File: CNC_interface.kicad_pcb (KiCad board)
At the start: 2 copper layers, 86.4 x 99.1 mm, 35 parts, among them J1 Conn_01x04_Male, J10 Conn_01x08, J11 Conn_01x08, J12 Conn_01x08, J13 Conn_01x08, J14 Conn_01x03_Male, J15 Conn_01x03_Male, J16 Conn_01x03_Male, J17 Conn_01x08, J18 Conn_01x10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

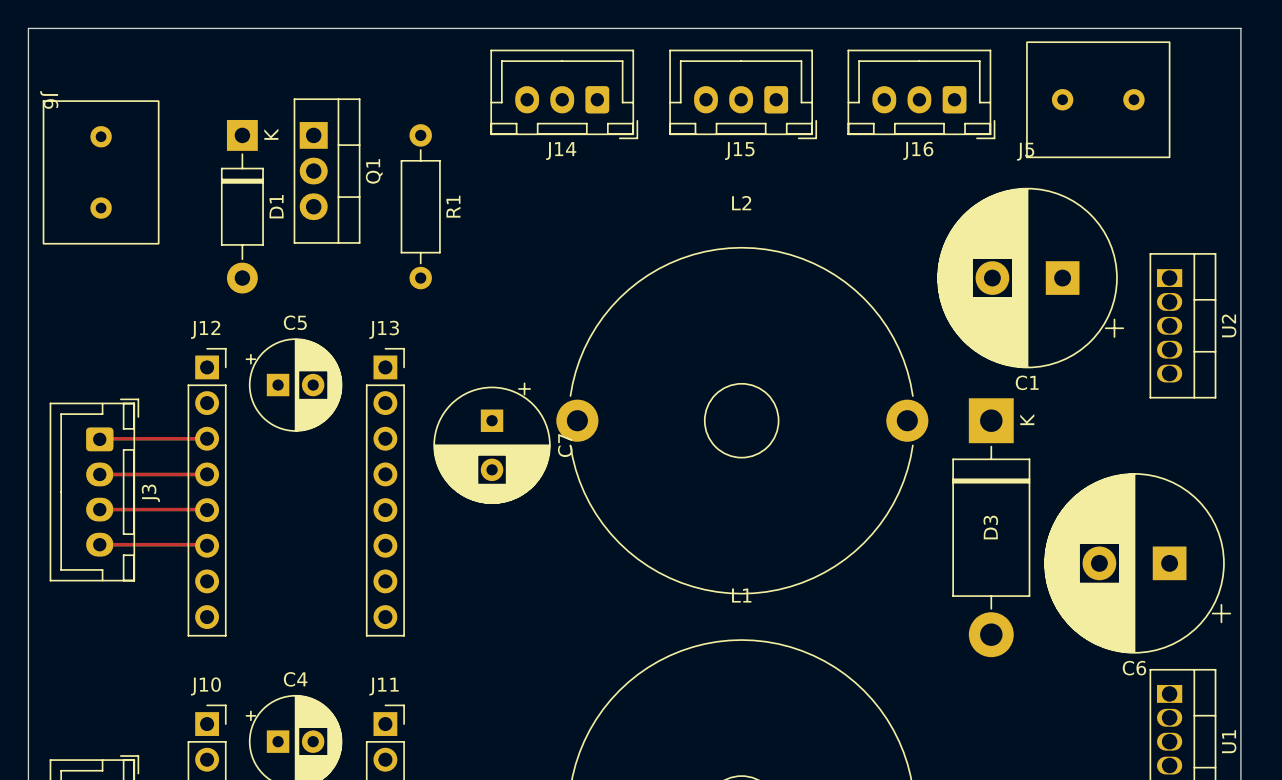
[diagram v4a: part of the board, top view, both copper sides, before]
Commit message: place first traces
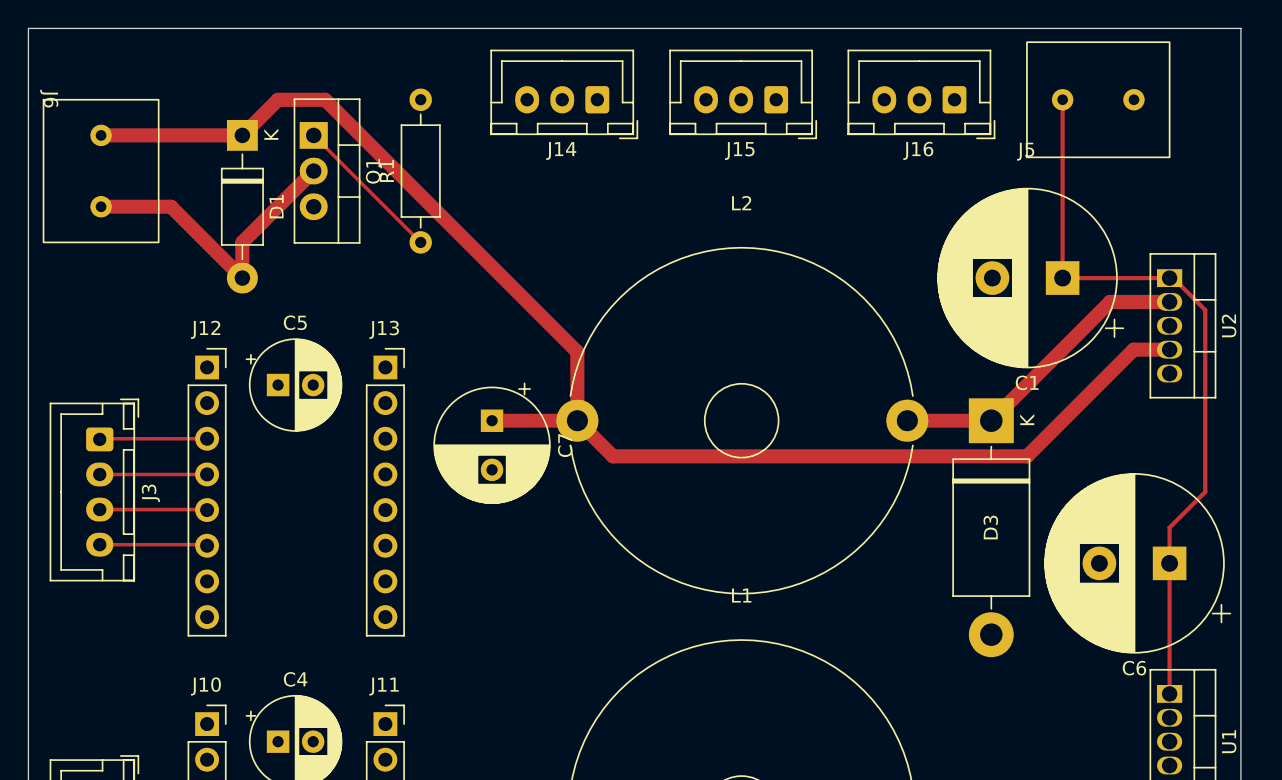
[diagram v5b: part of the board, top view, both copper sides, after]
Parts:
- moved R1 7.62 mm to (73.7, 45.7), turned to 90 degrees
- moved J6 0.09 mm to (46.8, 35.6)
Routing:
- net +12V: track 0.00 -> 99.8 mm
- net +24V: track 0.00 -> 52.2 mm
- net Net-(D3-Pad1): track 0.00 -> 22.2 mm
- net DC-: track 0.00 -> 21.9 mm
- net DCtrl: track 0.00 -> 10.8 mm
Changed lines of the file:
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@@
   )
   (setup
+    (stackup
+      (layer "F.SilkS" (type "Top Silk Screen"))
+      (layer "F.Paste" (type "Top Solder Paste"))
+      (layer "F.Mask" (type "Top Solder Mask") (thickness 0.01))
+      (layer "F.Cu" (type "copper") (thickness 0.035))
+      (layer "dielectric 1" (type "core") (thickness 1.51) (material "FR4") (epsilon_r 4.5) (loss_tangent 0.02))
+      (layer "B.Cu" (type "copper") (thickness 0.035))
+      (layer "B.Mask" (type "Bottom Solder Mask") (thickness 0.01))
+      (layer "B.Paste" (type "Bottom Solder Paste"))
+      (layer "B.SilkS" (type "Bottom Silk Screen"))
+      (copper_finish "None")
+      (dielectric_constraints no)
+    )
     (pad_to_mask_clearance 0)
     (pcbplotparams
@@
   )
   (footprint "CNC_interface:RS_pro_screw_terminal_P5.08_x2" (layer "F.Cu")
-    (at 46.795 35.655 -90)
+    (at 46.795 35.56 -90)
     (property "Sheetfile" "CNC_interface.kicad_sch")
     (property "Sheetname" "")
@@
   )
   (footprint "Resistor_THT:R_Axial_DIN0207_L6.3mm_D2.5mm_P10.16mm_Horizontal" (layer "F.Cu")
-    (at 73.66 38.1 -90)
+    (at 73.66 45.72 90)
     (descr "Resistor, Axial_DIN0207 series, Axial, Horizontal, pin pitch=10.16mm, 0.25W = 1/4W, length*diameter=6.3*2.5mm^2, http://cdn-reichelt.de/documents/datenblatt/B400/1_4W%23YAG.pdf")
     (tags "Resistor Axial_DIN0207 series Axial Horizontal pin pitch 10.16mm 0.25W = 1/4W length 6.3mm diameter 2.5mm")
@@
     (fp_line (start 0 0) (end 1.93 0) (layer "F.Fab") (width 0.1))
     (fp_line (start 1.93 -1.25) (end 1.93 1.25) (layer "F.Fab") (width 0.1))
-    (pad "1" thru_hole circle (at 0 0 270) (size 1.6 1.6) (drill 0.8) (layers *.Cu *.Mask)
+    (pad "1" thru_hole circle (at 0 0 90) (size 1.6 1.6) (drill 0.8) (layers *.Cu *.Mask)
       (net 41 "DCtrl") (pintype "passive"))
-    (pad "2" thru_hole oval (at 10.16 0 270) (size 1.6 1.6) (drill 0.8) (layers *.Cu *.Mask)
+    (pad "2" thru_hole oval (at 10.16 0 90) (size 1.6 1.6) (drill 0.8) (layers *.Cu *.Mask)
       (net 19 "GND") (pintype "passive"))
     (model "${KICAD6_3DMODEL_DIR}/Resistor_THT.3dshapes/R_Axial_DIN0207_L6.3mm_D2.5mm_P10.16mm_Horizontal.wrl"
@@
   (gr_line (start 45.72 129.54) (end 45.72 30.48) (layer "Edge.Cuts") (width 0.05))
   (gr_line (start 132.08 30.48) (end 132.08 129.54) (layer "Edge.Cuts") (width 0.05))
+  (segment (start 50.895 43.18) (end 55.88 43.18) (width 1) (layer "F.Cu") (net 1))
+  (segment (start 66.04 40.64) (end 60.96 45.72) (width 1) (layer "F.Cu") (net 1))
+  (segment (start 55.88 43.18) (end 60.96 48.26) (width 1) (layer "F.Cu") (net 1))
+  (segment (start 60.96 45.72) (end 60.96 48.26) (width 1) (layer "F.Cu") (net 1))
   (segment (start 50.8 119.26) (end 58.325 119.26) (width 0.25) (layer "F.Cu") (net 3))
   (segment (start 58.325 119.26) (end 58.445 119.38) (width 0.25) (layer "F.Cu") (net 3))
@@
   (segment (start 50.8 114.26) (end 58.405 114.26) (width 0.25) (layer "F.Cu") (net 5))
   (segment (start 50.8 111.76) (end 58.445 111.76) (width 0.25) (layer "F.Cu") (net 6))
+  (segment (start 127 48.26) (end 127.2625 48.26) (width 0.3) (layer "F.Cu") (net 8))
+  (segment (start 127.2625 48.26) (end 129.54 50.5375) (width 0.3) (layer "F.Cu") (net 8))
+  (segment (start 129.54 50.5375) (end 129.54 63.5) (width 0.3) (layer "F.Cu") (net 8))
+  (segment (start 119.38 35.56) (end 119.38 48.26) (width 0.3) (layer "F.Cu") (net 8))
+  (segment (start 129.54 63.5) (end 127 66.04) (width 0.3) (layer "F.Cu") (net 8))
+  (segment (start 127 66.04) (end 127 68.58) (width 0.3) (layer "F.Cu") (net 8))
+  (segment (start 127 77.88) (end 127 68.58) (width 0.3) (layer "F.Cu") (net 8))
+  (segment (start 119.38 48.26) (end 127 48.26) (width 0.3) (layer "F.Cu") (net 8))
+  (segment (start 114.3 58.42) (end 108.32 58.42) (width 1) (layer "F.Cu") (net 9))
+  (segment (start 122.76 49.96) (end 114.3 58.42) (width 1) (layer "F.Cu") (net 9))
+  (segment (start 127 49.96) (end 122.76 49.96) (width 1) (layer "F.Cu") (net 9))
   (segment (start 58.37 92.65) (end 58.445 92.725) (width 0.25) (layer "F.Cu") (net 14))
   (segment (start 50.8 92.65) (end 58.37 92.65) (width 0.25) (layer "F.Cu") (net 14))
@@
   (segment (start 50.8 59.75) (end 50.845 59.705) (width 0.25) (layer "F.Cu") (net 27))
   (segment (start 50.845 59.705) (end 58.445 59.705) (width 0.25) (layer "F.Cu") (net 27))
+  (segment (start 73.66 45.72) (end 66.04 38.1) (width 0.25) (layer "F.Cu") (net 41))
+  (segment (start 124.44 53.36) (end 116.84 60.96) (width 1) (layer "F.Cu") (net 61))
+  (segment (start 127 53.36) (end 124.44 53.36) (width 1) (layer "F.Cu") (net 61))
+  (segment (start 84.82 53.528478) (end 66.851522 35.56) (width 1) (layer "F.Cu") (net 61))
+  (segment (start 84.82 58.42) (end 78.74 58.42) (width 1) (layer "F.Cu") (net 61))
+  (segment (start 66.851522 35.56) (end 63.5 35.56) (width 1) (layer "F.Cu") (net 61))
+  (segment (start 87.36 60.96) (end 84.82 58.42) (width 1) (layer "F.Cu") (net 61))
+  (segment (start 60.96 38.1) (end 50.895 38.1) (width 1) (layer "F.Cu") (net 61))
+  (segment (start 116.84 60.96) (end 87.36 60.96) (width 1) (layer "F.Cu") (net 61))
+  (segment (start 63.5 35.56) (end 60.96 38.1) (width 1) (layer "F.Cu") (net 61))
+  (segment (start 84.82 58.42) (end 84.82 53.528478) (width 1) (layer "F.Cu") (net 61))
   (group "" (id 11578d5e-03e8-4330-bf12-98756cee3ec6)
     (members

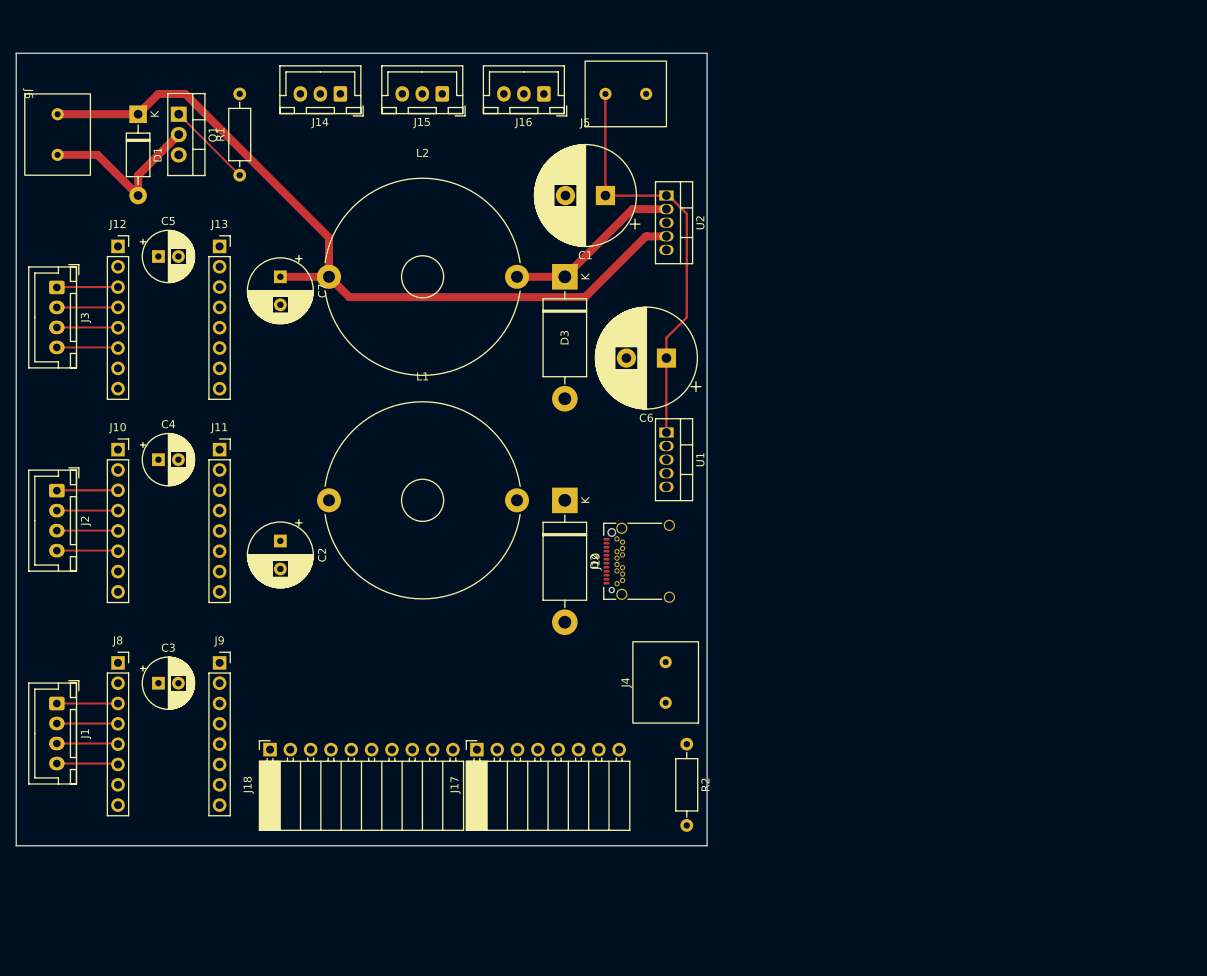
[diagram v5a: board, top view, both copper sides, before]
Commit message: route pcb + GND floorplan
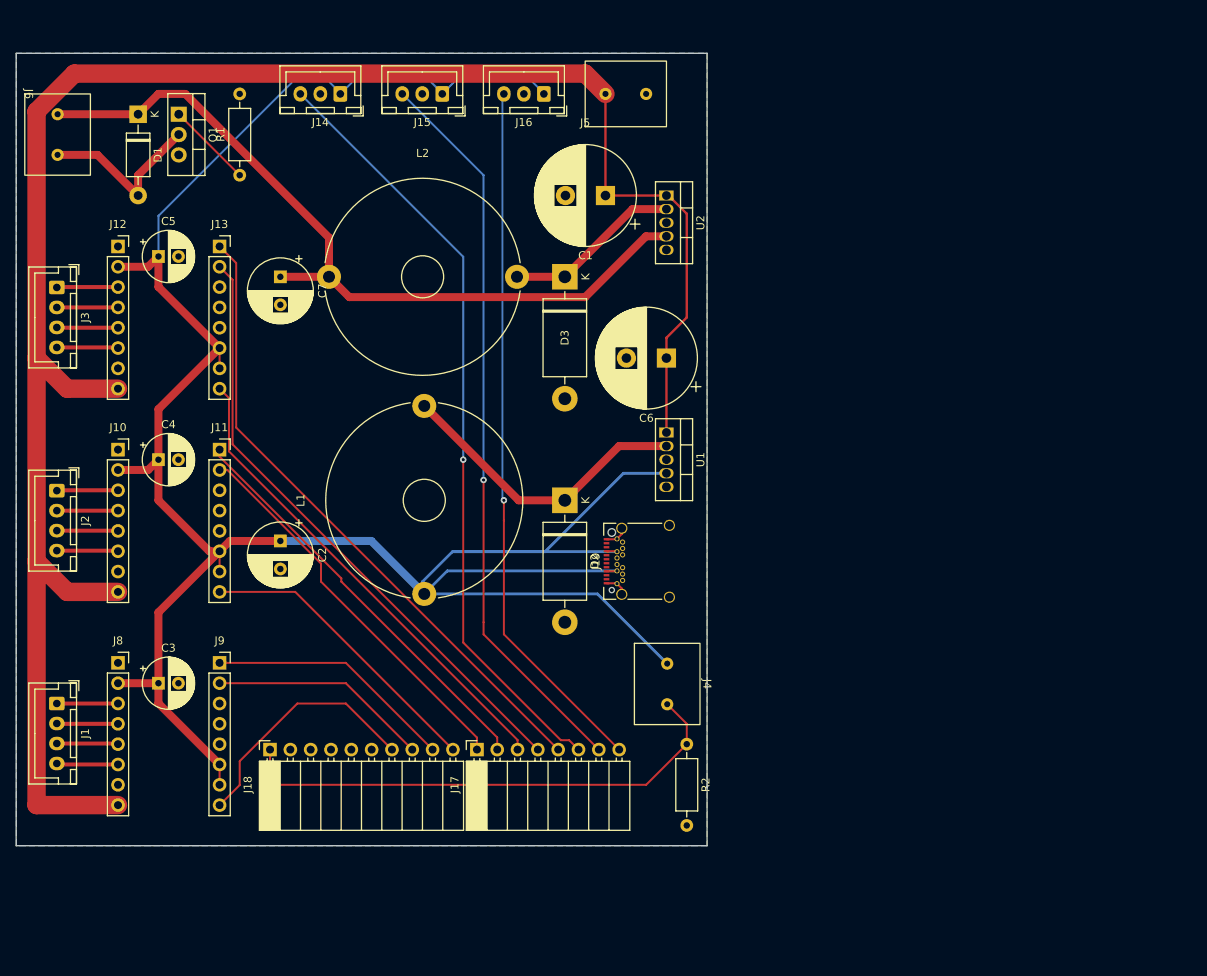
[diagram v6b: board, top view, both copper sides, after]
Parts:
- moved L1 16.7 mm to (96.5, 98.1), turned to 90 degrees
- moved J4 12.8 mm to (123.0, 104.2), turned to -90 degrees
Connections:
- J17 pad 3: ENx -> ENz
- J17 pad 4: STEPx -> STEPz
- J17 pad 5: DIRx -> DIRz
- J18 pad 7: ENz -> ENx
- J18 pad 8: STEPz -> STEPx
- J18 pad 9: DIRz -> DIRx
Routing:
- net +5V: track 0.00 -> 319.0 mm
- net +24V: track 52.2 -> 246.8 mm
- net Lx: track 0.00 -> 97.0 mm, vias 0 -> 1
- net Ly: track 0.00 -> 92.1 mm, vias 0 -> 1
- net Lz: track 0.00 -> 88.1 mm, vias 0 -> 1
- net DIRz: track 0.00 -> 80.4 mm
- net STEPz: track 0.00 -> 76.8 mm
- net CONT: track 0.00 -> 63.8 mm
- net ENz: track 0.00 -> 60.5 mm
- net DIRy: track 0.00 -> 51.9 mm
- net STEPy: track 0.00 -> 48.8 mm
- net Net-(D2-Pad1): track 0.00 -> 38.0 mm
- net ENy: track 0.00 -> 37.3 mm
- net DIRx: track 0.00 -> 31.1 mm
- net ENx: track 0.00 -> 30.9 mm
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- added copper zone on B.Cu, net GND

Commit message: Finish routing
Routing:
- net DCtrl: track 10.8 -> 89.4 mm
- net GND: track 5.82 -> 24.3 mm
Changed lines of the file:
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@@
   (segment (start 69.865 92.725) (end 63.5 86.36) (width 1) (layer "F.Cu") (net 2))
   (segment (start 96.73 98.06) (end 99.61 95.18) (width 0.35) (layer "B.Cu") (net 2))
-  (segment (start 98.98 35.48) (end 98.98 35.56) (width 0.25) (layer "B.Cu") (net 2))
   (segment (start 63.5 55.88) (end 63.5 50.8) (width 0.25) (layer "B.Cu") (net 2))
   (segment (start 96.73 98.06) (end 96.52 97.85) (width 0.35) (layer "B.Cu") (net 2))
-  (segment (start 96.52 33.02) (end 98.98 35.48) (width 0.25) (layer "B.Cu") (net 2))
   (segment (start 118.38 98.06) (end 127.095 106.775) (width 0.35) (layer "B.Cu") (net 2))
   (segment (start 99.61 95.18) (end 120.82 95.18) (width 0.35) (layer "B.Cu") (net 2))
@@
   (segment (start 83.82 33.02) (end 86.24 35.44) (width 0.25) (layer "B.Cu") (net 2))
   (segment (start 86.24 35.44) (end 86.24 35.56) (width 0.25) (layer "B.Cu") (net 2))
+  (segment (start 96.52 33.02) (end 98.98 35.48) (width 0.25) (layer "B.Cu") (net 2))
   (segment (start 81.28 33.02) (end 83.82 33.02) (width 0.25) (layer "B.Cu") (net 2))
+  (segment (start 88.78 33.02) (end 96.52 33.02) (width 0.25) (layer "B.Cu") (net 2))
   (segment (start 96.52 96.52) (end 100.26 92.78) (width 0.35) (layer "B.Cu") (net 2))
-  (segment (start 86.24 35.56) (end 88.78 33.02) (width 0.25) (layer "B.Cu") (net 2))
   (segment (start 96.73 98.06) (end 90.11 91.44) (width 1) (layer "B.Cu") (net 2))
   (segment (start 96.52 97.85) (end 96.52 96.52) (width 0.35) (layer "B.Cu") (net 2))
-  (segment (start 88.78 33.02) (end 96.52 33.02) (width 0.25) (layer "B.Cu") (net 2))
+  (segment (start 86.24 35.56) (end 88.78 33.02) (width 0.25) (layer "B.Cu") (net 2))
   (segment (start 109.22 33.02) (end 111.68 35.48) (width 0.25) (layer "B.Cu") (net 2))
   (segment (start 111.68 35.48) (end 111.68 35.56) (width 0.25) (layer "B.Cu") (net 2))
   (segment (start 111.829022 92.78) (end 121.629022 82.98) (width 0.35) (layer "B.Cu") (net 2))
+  (segment (start 98.98 35.48) (end 98.98 35.56) (width 0.25) (layer "B.Cu") (net 2))
   (segment (start 58.445 119.38) (end 50.8 119.38) (width 0.5) (layer "F.Cu") (net 3))
   (segment (start 58.325 119.26) (end 58.445 119.38) (width 0.25) (layer "F.Cu") (net 3))
@@
   (segment (start 100.31 117.52) (end 80.595 97.805) (width 0.25) (layer "F.Cu") (net 18))
   (segment (start 80.595 97.805) (end 71.145 97.805) (width 0.25) (layer "F.Cu") (net 18))
+  (segment (start 96.48 35.56) (end 99.02 38.1) (width 0.25) (layer "F.Cu") (net 19))
   (segment (start 120.77 96.73) (end 120.82 96.78) (width 0.25) (layer "F.Cu") (net 19))
   (segment (start 119.51 96.73) (end 120.77 96.73) (width 0.25) (layer "F.Cu") (net 19))
+  (segment (start 99.02 38.1) (end 106.64 38.1) (width 0.25) (layer "F.Cu") (net 19))
   (segment (start 121.42 97.38) (end 121.42 98.11) (width 0.25) (layer "F.Cu") (net 19))
   (segment (start 119.51 91.23) (end 120.77 91.23) (width 0.25) (layer "F.Cu") (net 19))
   (segment (start 120.82 96.78) (end 121.42 97.38) (width 0.25) (layer "F.Cu") (net 19))
   (segment (start 121.42 90.58) (end 121.42 89.85) (width 0.25) (layer "F.Cu") (net 19))
+  (segment (start 106.64 38.1) (end 109.18 35.56) (width 0.25) (layer "F.Cu") (net 19))
   (segment (start 120.82 91.18) (end 121.42 90.58) (width 0.25) (layer "F.Cu") (net 19))
   (segment (start 120.77 91.23) (end 120.82 91.18) (width 0.25) (layer "F.Cu") (net 19))
+  (segment (start 83.74 35.56) (end 83.82 35.56) (width 0.25) (layer "B.Cu") (net 19))
+  (segment (start 83.82 35.56) (end 86.36 38.1) (width 0.25) (layer "B.Cu") (net 19))
   (segment (start 103.31 117.52) (end 103.31 116.01) (width 0.25) (layer "F.Cu") (net 22))
   (segment (start 103.31 116.01) (end 83.82 96.52) (width 0.25) (layer "F.Cu") (net 22))
@@
   (segment (start 127 79.58) (end 121.08 79.58) (width 1) (layer "F.Cu") (net 40))
   (segment (start 73.66 45.72) (end 66.04 38.1) (width 0.25) (layer "F.Cu") (net 41))
+  (segment (start 90.15 117.52) (end 73.66 101.03) (width 0.25) (layer "B.Cu") (net 41))
+  (segment (start 73.66 101.03) (end 73.66 45.72) (width 0.25) (layer "B.Cu") (net 41))
   (segment (start 78.74 121.92) (end 124.46 121.92) (width 0.25) (layer "F.Cu") (net 47))
   (segment (start 129.54 116.84) (end 129.54 114.3) (width 0.25) (layer "F.Cu") (net 47))

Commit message: finish routing
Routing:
- net GND: track 24.3 -> 20.8 mm
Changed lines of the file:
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@@
   (segment (start 100.31 117.52) (end 80.595 97.805) (width 0.25) (layer "F.Cu") (net 18))
   (segment (start 80.595 97.805) (end 71.145 97.805) (width 0.25) (layer "F.Cu") (net 18))
-  (segment (start 96.48 35.56) (end 99.02 38.1) (width 0.25) (layer "F.Cu") (net 19))
   (segment (start 120.77 96.73) (end 120.82 96.78) (width 0.25) (layer "F.Cu") (net 19))
+  (segment (start 96.48 35.6) (end 96.48 35.56) (width 0.25) (layer "F.Cu") (net 19))
   (segment (start 119.51 96.73) (end 120.77 96.73) (width 0.25) (layer "F.Cu") (net 19))
-  (segment (start 99.02 38.1) (end 106.64 38.1) (width 0.25) (layer "F.Cu") (net 19))
+  (segment (start 93.98 38.1) (end 96.48 35.6) (width 0.25) (layer "F.Cu") (net 19))
+  (segment (start 86.28 38.1) (end 93.98 38.1) (width 0.25) (layer "F.Cu") (net 19))
+  (segment (start 83.74 35.56) (end 86.28 38.1) (width 0.25) (layer "F.Cu") (net 19))
   (segment (start 121.42 97.38) (end 121.42 98.11) (width 0.25) (layer "F.Cu") (net 19))
   (segment (start 119.51 91.23) (end 120.77 91.23) (width 0.25) (layer "F.Cu") (net 19))
   (segment (start 120.82 96.78) (end 121.42 97.38) (width 0.25) (layer "F.Cu") (net 19))
   (segment (start 121.42 90.58) (end 121.42 89.85) (width 0.25) (layer "F.Cu") (net 19))
-  (segment (start 106.64 38.1) (end 109.18 35.56) (width 0.25) (layer "F.Cu") (net 19))
   (segment (start 120.82 91.18) (end 121.42 90.58) (width 0.25) (layer "F.Cu") (net 19))
   (segment (start 120.77 91.23) (end 120.82 91.18) (width 0.25) (layer "F.Cu") (net 19))
   (segment (start 83.74 35.56) (end 83.82 35.56) (width 0.25) (layer "B.Cu") (net 19))
-  (segment (start 83.82 35.56) (end 86.36 38.1) (width 0.25) (layer "B.Cu") (net 19))
   (segment (start 103.31 117.52) (end 103.31 116.01) (width 0.25) (layer "F.Cu") (net 22))
   (segment (start 103.31 116.01) (end 83.82 96.52) (width 0.25) (layer "F.Cu") (net 22))
